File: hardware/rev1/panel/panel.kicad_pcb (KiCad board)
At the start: 2 copper layers, 40.3 x 128 mm, 13 parts

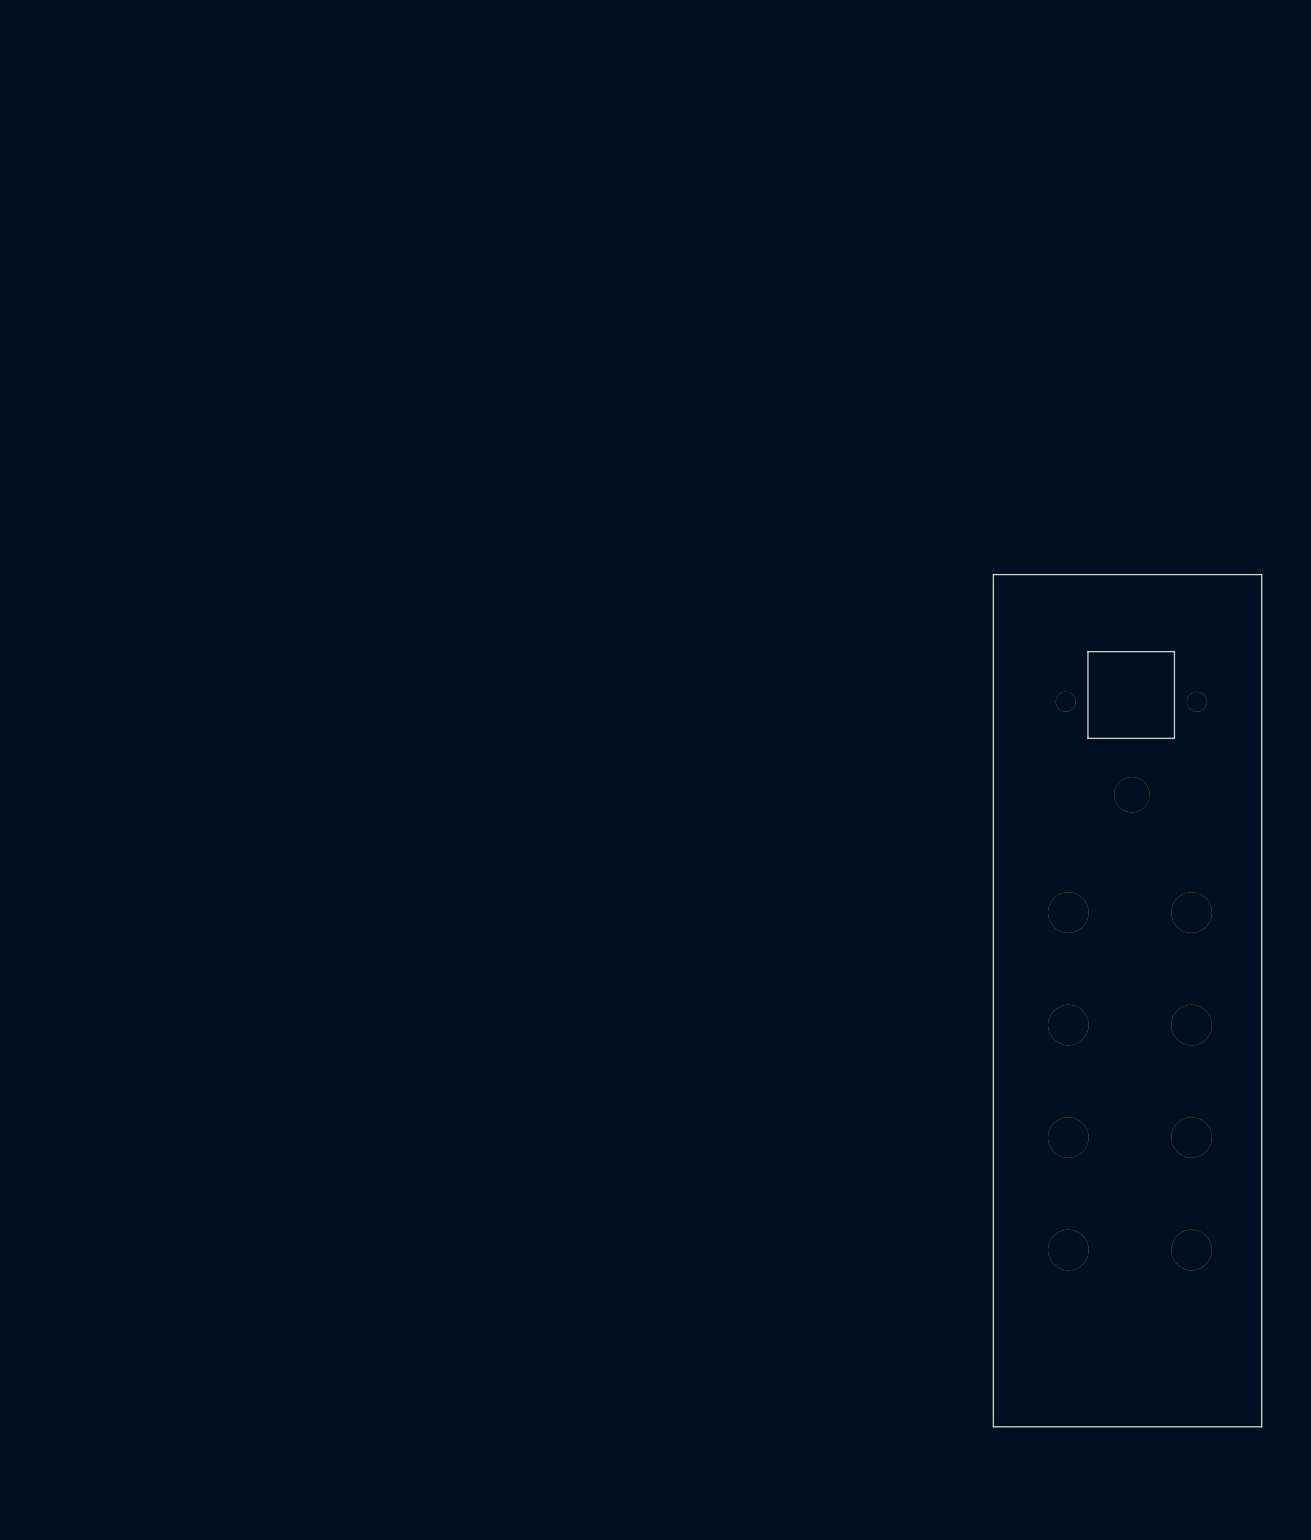
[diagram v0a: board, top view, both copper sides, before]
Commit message: Add blank panel
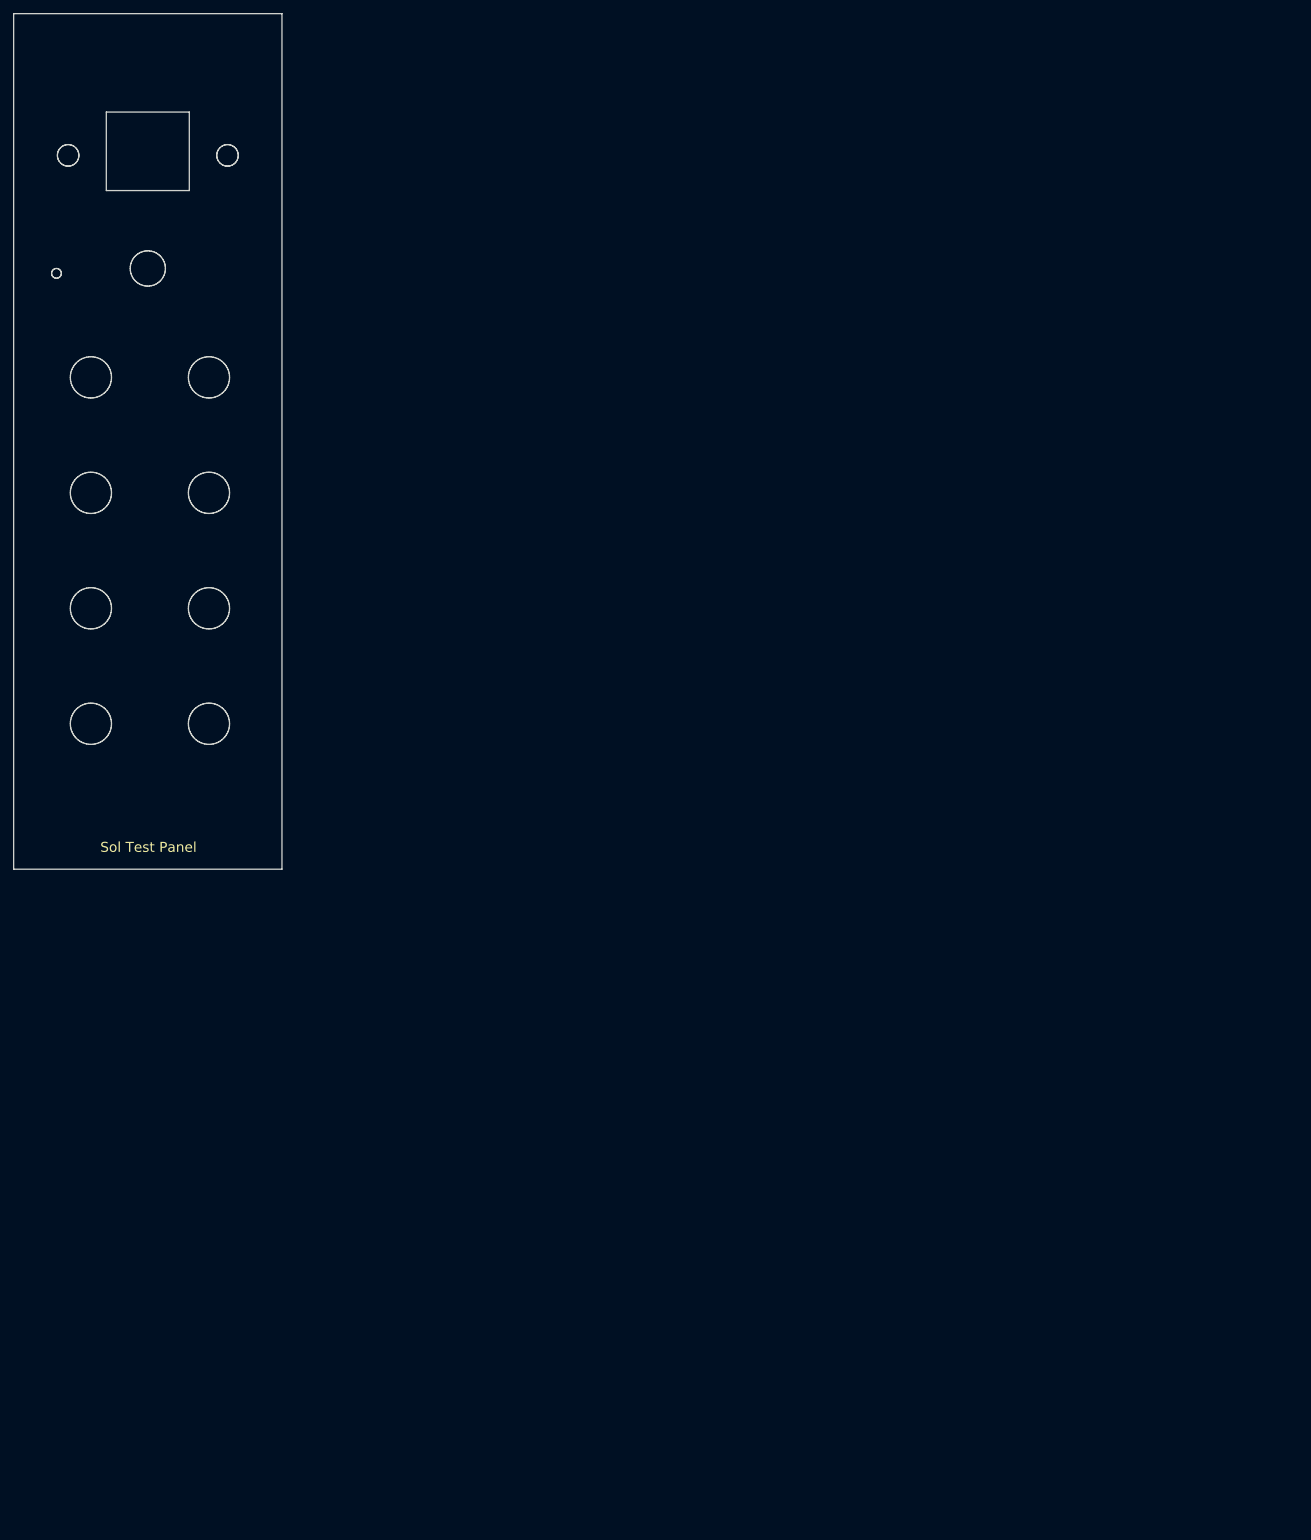
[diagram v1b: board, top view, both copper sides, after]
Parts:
- removed the   at (132.0, 23.0)
- removed the   at (132.0, 145.0)
- removed ? (x11): , Wire_Pads:SolderWirePad_single_0-8mmDrill
- added  : , panel:MountingHoleEurorackSlotM3, F.Cu at (-15.1, -61.2)
- added  : , panel:MountingHoleEurorackSlotM3, F.Cu at (-15.1, 61.2)
- added G***: LOGO, LOGO, F.Cu at (0.00, 0.00)
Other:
- board size 40.3 x 128 mm -> 40.3 x 128.5 mm
- board text added: "Sol Test Panel"

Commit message: Update panel and gerbers
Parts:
- removed the   at (-15.1, -61.2)
- removed the   at (-15.1, 61.2)
- removed the G*** at (0.00, 0.00)
- added  : , panel:MountingHoleEurorackSlotM3, F.Cu at (139.9, 37.5)
- added  : , panel:MountingHoleEurorackSlotM3, F.Cu at (139.9, 159.9)
- added G*** (x3): LOGO, LOGO, F.Cu at (152.5, 98.7)
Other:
- outline, holes or cut-outs redrawn
- board text removed: "Sol Test Panel"

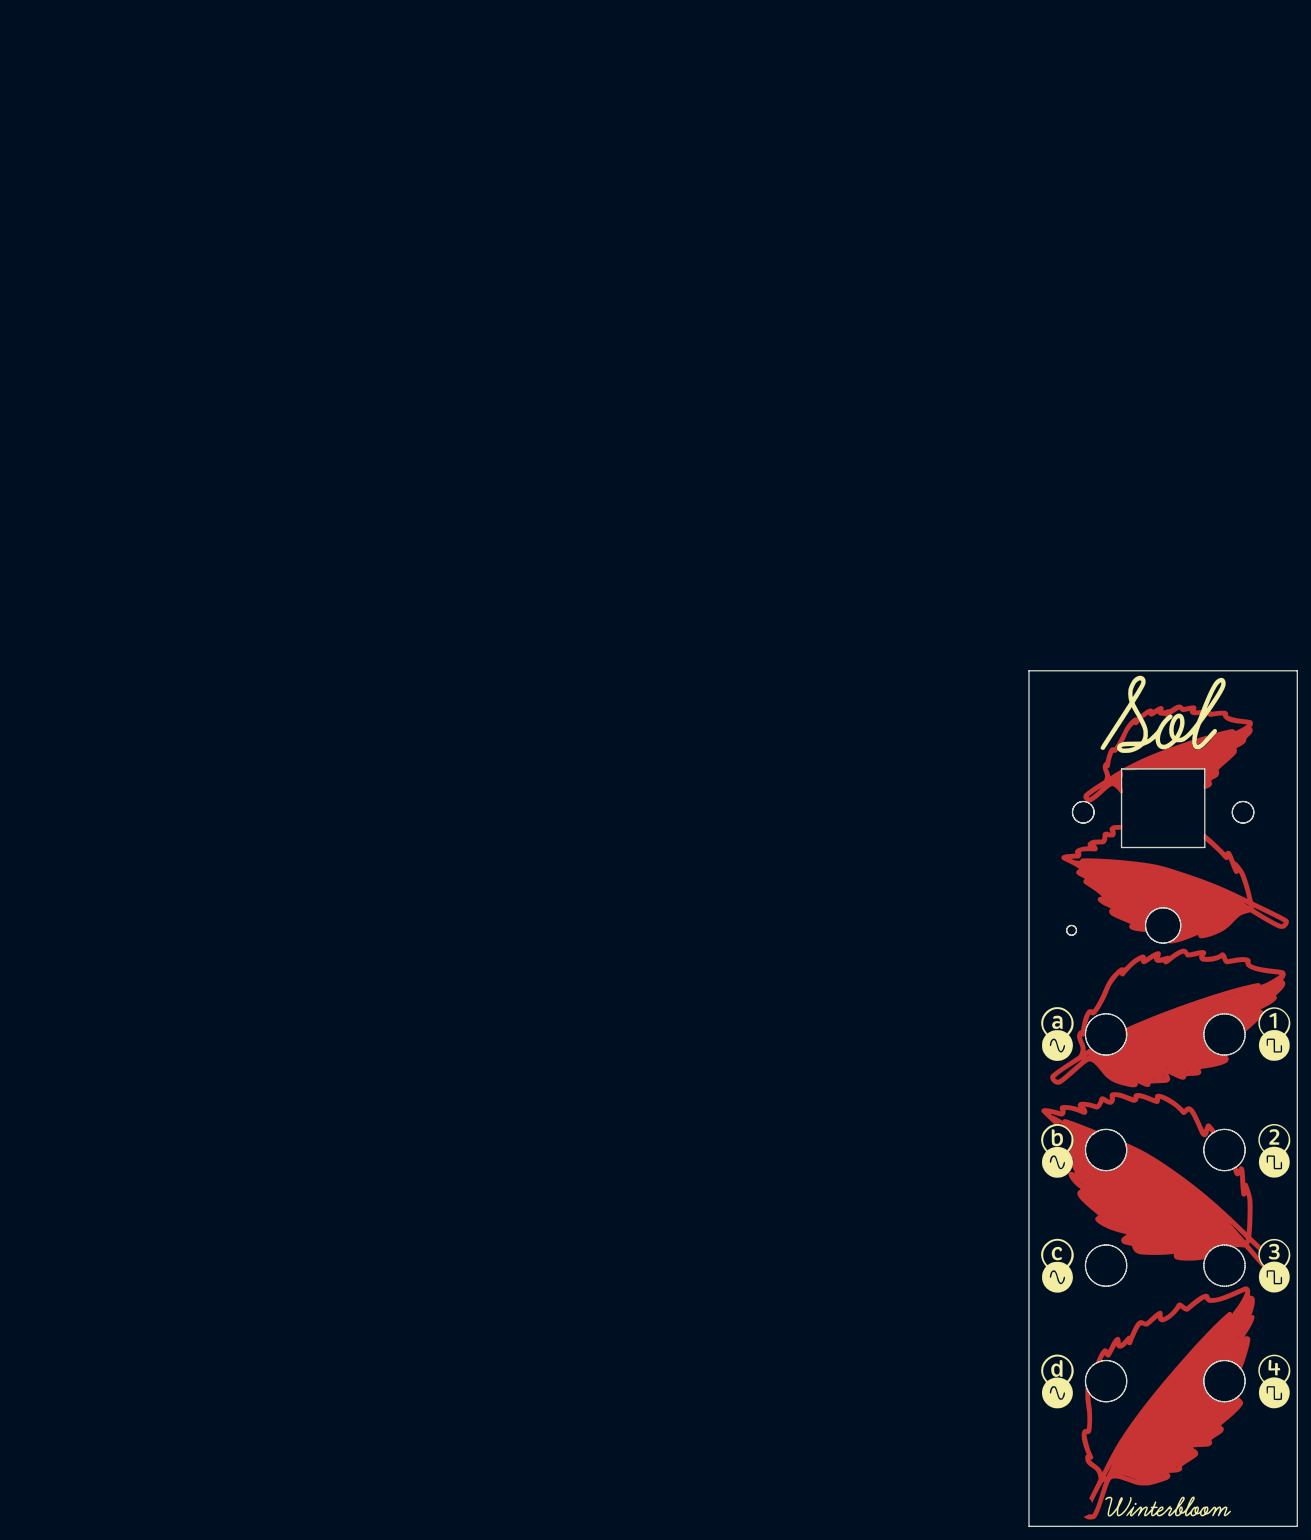
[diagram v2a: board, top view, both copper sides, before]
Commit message: Update panel with new logo
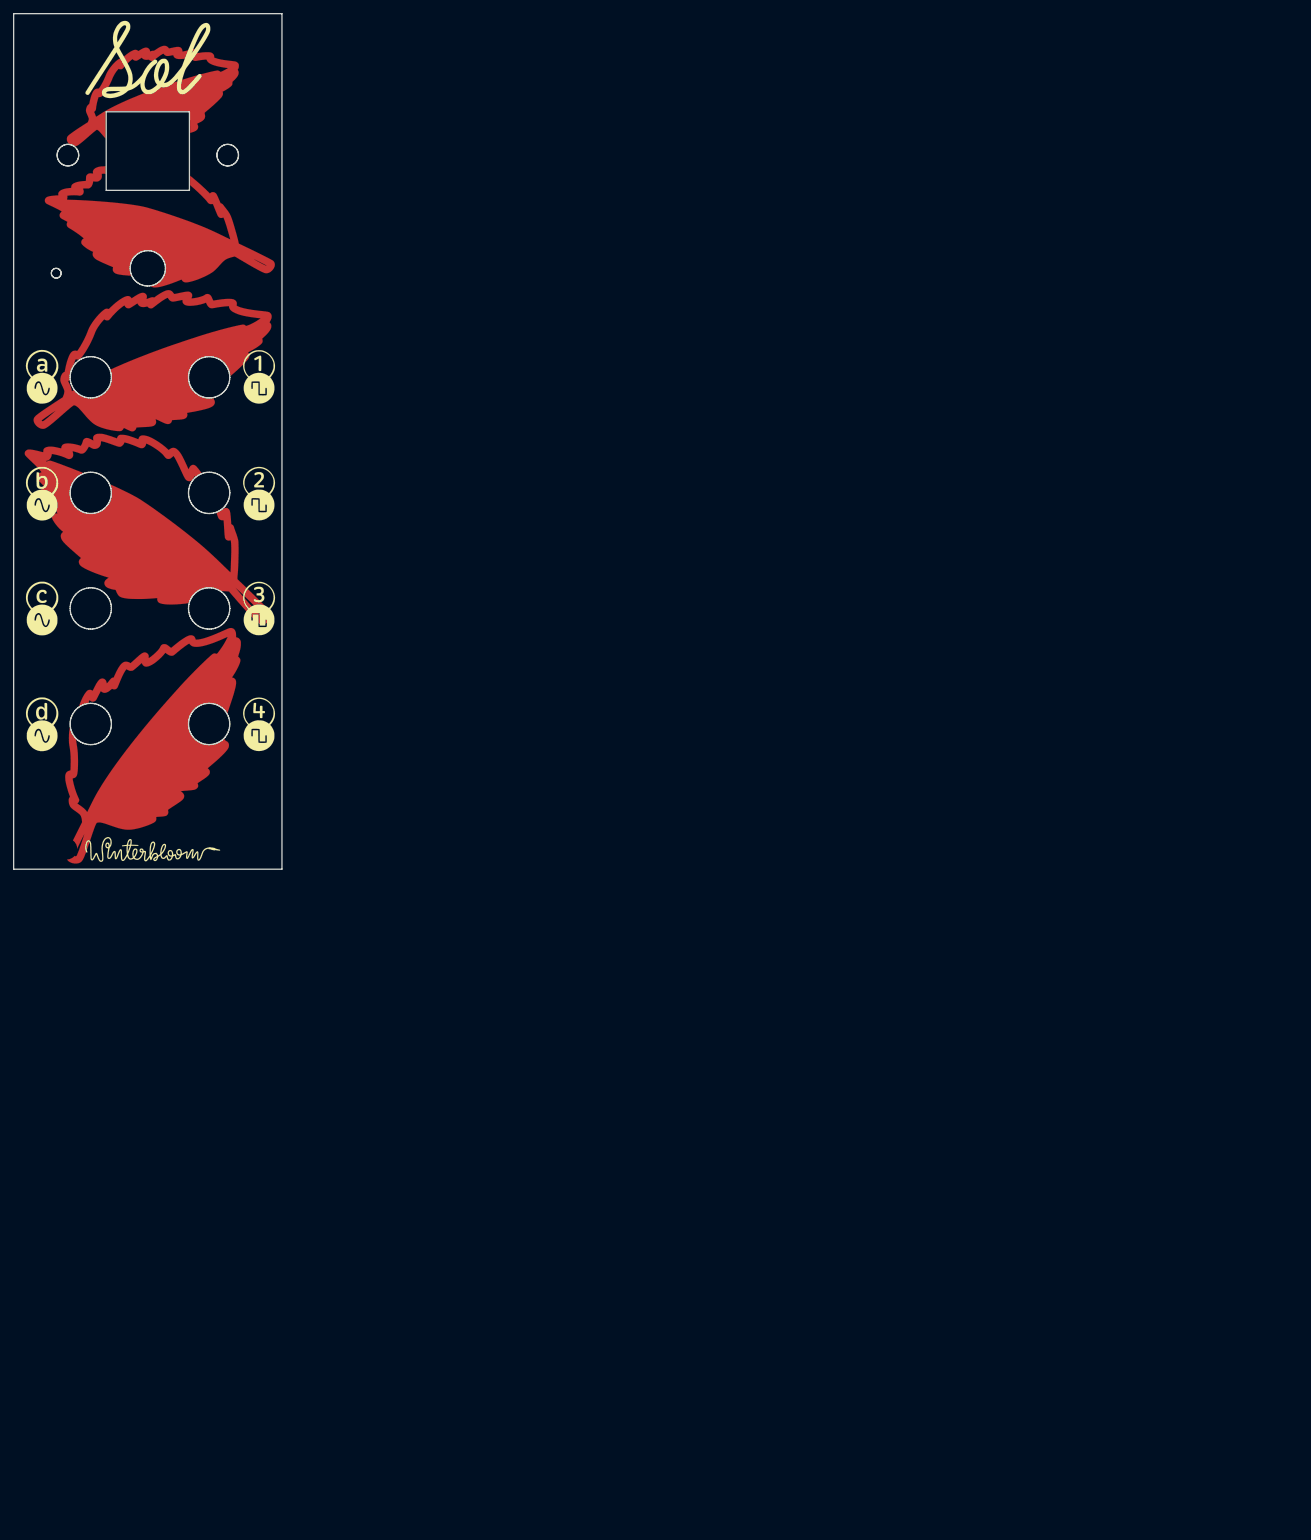
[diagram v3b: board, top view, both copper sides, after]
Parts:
- removed the   at (139.9, 37.5)
- removed the   at (139.9, 159.9)
- removed the G*** at (152.5, 98.7) (x3)
- added  : , panel:MountingHoleEurorackSlotM3, F.Cu at (-12.6, -61.2)
- added  : , panel:MountingHoleEurorackSlotM3, F.Cu at (-12.6, 61.2)
- added G*** (x3): LOGO, LOGO, F.Cu at (0.00, 0.00)
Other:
- outline, holes or cut-outs redrawn

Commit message: Update all gerbes for latest PCB revisions
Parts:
- removed the G*** at (0.00, 0.00) (x3)
- added G*** (x3): LOGO, LOGO, F.Cu at (0.00, 0.00)
- added Ref**: Val**, panel:ermine, B.Cu at (0.60, 51.7)
